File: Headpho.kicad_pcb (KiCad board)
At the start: 2 copper layers, 20 x 106.7 mm, 39 parts, among them IC1 NJM4556AD, IC2 NJM4556AD, J1 IN L, J2 IN R, J3 Eurorack_Power_10pin_Unshroud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, J4 LINE OUT L, J5 OUT LR, J6 LINE OUT R, U1 LME49720, U2 LME49720

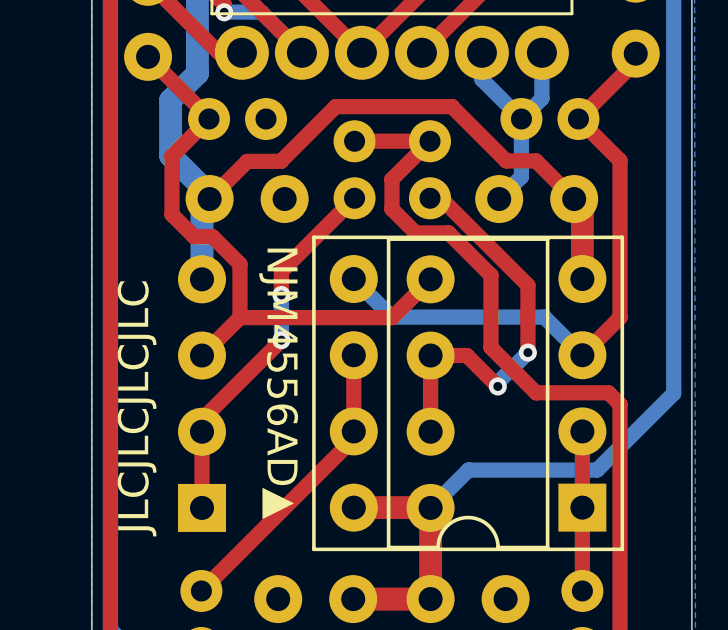
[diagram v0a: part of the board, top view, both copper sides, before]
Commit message: fixed silkscreening issues before sending for new boards
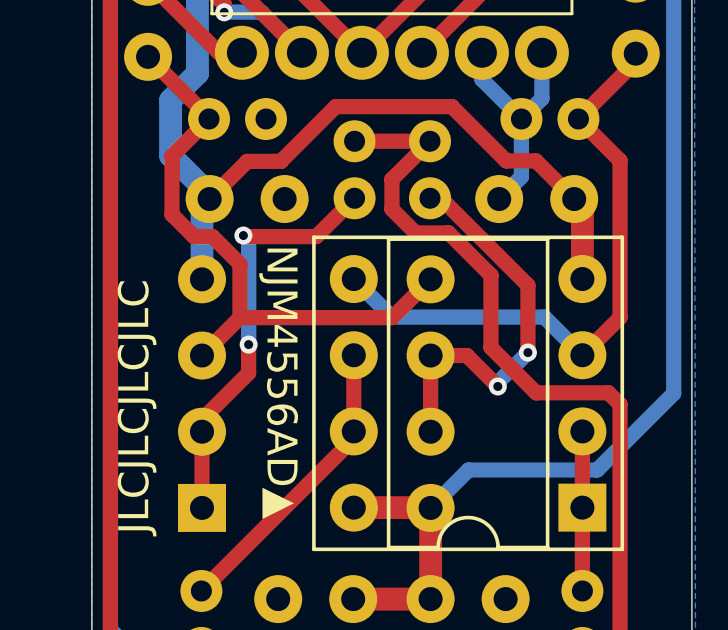
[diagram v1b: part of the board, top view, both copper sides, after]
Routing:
- net Net-(IC2-A_-INPUT): track 12.4 -> 14.0 mm
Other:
- board text added: "HEADPHO"
- board text added: "github.com/fablabnk/SynthLabProjects"
- board text removed: "`HEADPHO`"
- board text removed: "https://www.github.com/ fablabnk/SynthLabProjects"
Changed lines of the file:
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@@
 		)
 		(property "Silkscreen Value" "◀100k"
-			(at 0.889 -4.191 -90)
+			(at 0.889 -3.5052 -90)
 			(unlocked yes)
 			(layer "B.SilkS")
@@
 			)
 		)
-		(property "Silkscreen Value" "104▲"
-			(at 1.504 -2.286 0)
+		(property "Silkscreen Value" "104▶"
+			(at 2.6724 3.4544 90)
 			(unlocked yes)
 			(layer "B.SilkS")
@@
 			)
 		)
-		(property "Silkscreen Value" "1Ω▼"
-			(at 3.2258 -0.6604 0)
+		(property "Silkscreen Value" "▼1Ω"
+			(at 3.2258 -0.4826 0)
 			(unlocked yes)
 			(layer "B.SilkS")
@@
 		)
 		(property "Silkscreen Value" "1Ω▼"
-			(at 3.2258 0.635 0)
+			(at 3.2258 0.4826 0)
 			(unlocked yes)
 			(layer "B.SilkS")
@@
 		)
 		(property "Silkscreen Value" "◀100k"
-			(at 1.159 4.191 -90)
+			(at 1.159 3.5052 -90)
 			(unlocked yes)
 			(layer "B.SilkS")
@@
 		)
 		(property "Silkscreen Value" "100k▼"
-			(at -1 -3.556 90)
+			(at -1.4064 -1.3208 90)
 			(unlocked yes)
 			(layer "B.SilkS")
@@
 			)
 		)
-		(property "Silkscreen Value" "104▼"
-			(at 4.064 1.27 90)
+		(property "Silkscreen Value" "104▶"
+			(at 0.0816 -3.175 -90)
 			(unlocked yes)
 			(layer "B.SilkS")
@@
 			)
 		)
-		(property "Silkscreen Value" "◀104"
+		(property "Silkscreen Value" "▼104"
 			(at 4.151 -1.016 -90)
 			(unlocked yes)
@@
 			)
 		)
-		(property "Silkscreen Value" "1Ω"
-			(at 4.08 0.254 -90)
+		(property "Silkscreen Value" "1Ω▶"
+			(at 4.2324 0.4572 -90)
 			(unlocked yes)
 			(layer "B.SilkS")
@@
 			)
 		)
-		(property "Silkscreen Value" "100k▶"
-			(at -1.635 -2.286 0)
+		(property "Silkscreen Value" "100k▲"
+			(at -0.8984 -1.6764 0)
 			(unlocked yes)
 			(layer "B.SilkS")
@@
 		)
 		(property "Silkscreen Value" "100k▼"
-			(at 4.826 1.016 -90)
+			(at 3.6068 1.8796 -90)
 			(unlocked yes)
 			(layer "B.SilkS")
@@
 		)
 		(property "Silkscreen Value" "100k▲"
-			(at 4.821 -1.016 -90)
+			(at 3.3732 -1.4224 -90)
 			(unlocked yes)
 			(layer "B.SilkS")
@@
 			)
 		)
-		(property "Silkscreen Value" "104▲"
-			(at 4.298 -1.27 90)
+		(property "Silkscreen Value" "104▶"
+			(at 0.0308 3.1242 -90)
 			(unlocked yes)
 			(layer "B.SilkS")
@@
 			)
 		)
-		(property "Silkscreen Value" "1Ω"
-			(at 4.207 -0.508 -90)
+		(property "Silkscreen Value" "1Ω▶"
+			(at 4.2832 -0.6096 270)
 			(unlocked yes)
 			(layer "B.SilkS")
@@
 	)
 	(gr_text "STEREO HEADPHONE AMP"
-		(at 70.4596 55.626 0)
+		(at 70.4596 55.7554 0)
 		(layer "B.SilkS")
 		(effects
@@
 		)
 	)
-	(gr_text "`HEADPHO`"
-		(at 64.8462 52.451 0)
+	(gr_text "HEADPHO"
+		(at 64.4652 52.4534 0)
 		(layer "B.SilkS")
 		(effects
@@
 		)
 	)
-	(gr_text "PCB BY\n42 BERLIN\nSYNTHLAB\n"
-		(at 51.2318 157.2514 270)
+	(gr_text "PCB BY 42 BERLIN SYNTHLAB"
+		(at 53.086 156.949 270)
 		(layer "B.SilkS")
 		(effects
@@
 		)
 	)
-	(gr_text "https://www.github.com/\nfablabnk/SynthLabProjects"
-		(at 51.2318 148.7932 270)
+	(gr_text "github.com/fablabnk/SynthLabProjects"
+		(at 51.7144 156.8474 270)
 		(layer "B.SilkS")
 		(effects
@@
 	)
 	(segment
-		(start 57.277 117.349)
-		(end 57.277 116.563)
+		(start 54.63 121.504)
+		(end 54.63 121.907)
 		(width 0.508)
 		(layer "F.Cu")
@@
 	)
 	(segment
-		(start 54.63 121.907)
+		(start 58.436 115.404)
+		(end 59.7154 114.1246)
+		(width 0.508)
+		(layer "F.Cu")
+		(net 27)
+	)
+	(segment
+		(start 56.1848 119.9492)
 		(end 54.63 121.504)
 		(width 0.508)
@@
 	)
 	(segment
+		(start 56.046742 115.404)
+		(end 58.436 115.404)
+		(width 0.508)
+		(layer "F.Cu")
+		(net 27)
+	)
+	(segment
 		(start 54.63 121.907)
 		(end 54.63 124.447)
@@
 	)
 	(segment
-		(start 54.63 121.504)
-		(end 57.277 118.857)
+		(start 56.1848 119.0014)
+		(end 56.1848 119.9492)
 		(width 0.508)
 		(layer "F.Cu")
@@
 	)
 	(segment
-		(start 57.277 116.563)
-		(end 59.7154 114.1246)
+		(start 56.009471 115.366729)
+		(end 56.046742 115.404)
 		(width 0.508)
 		(layer "F.Cu")
@@
 	)
 	(via
-		(at 57.277 118.857)
+		(at 56.1848 119.0014)
 		(size 0.6)
 		(drill 0.3)
@@
 	)
 	(via
-		(at 57.277 117.349)
+		(at 56.009471 115.366729)
 		(size 0.6)
 		(drill 0.3)
@@
 	)
 	(segment
-		(start 57.277 118.857)
-		(end 57.277 117.349)
+		(start 56.1848 115.542058)
+		(end 56.009471 115.366729)
+		(width 0.508)
+		(layer "B.Cu")
+		(net 27)
+	)
+	(segment
+		(start 56.1848 119.0014)
+		(end 56.1848 115.542058)
 		(width 0.508)
 		(layer "B.Cu")
